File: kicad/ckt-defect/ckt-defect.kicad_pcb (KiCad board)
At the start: 2 copper layers, 99.1 x 61 mm, 67 parts, among them J1 Screw_Terminal_01x02, J10 Micro_SD_Card_Det_Hirose_DM3AT, J11 690-005-299-043, J12 SM04B-SRSS, J2 SM04B-SRSS, J3 SM04B-SRSS, J4 SM04B-SRSS, J5 SM04B-SRSS, J6 SM04B-SRSS, J7 SM04B-SRSS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

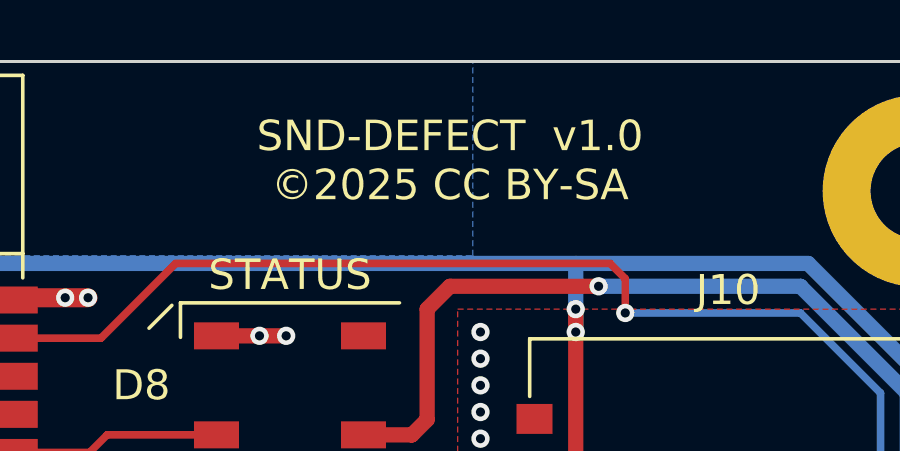
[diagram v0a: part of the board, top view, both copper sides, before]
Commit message: Renamed to ckt-defect
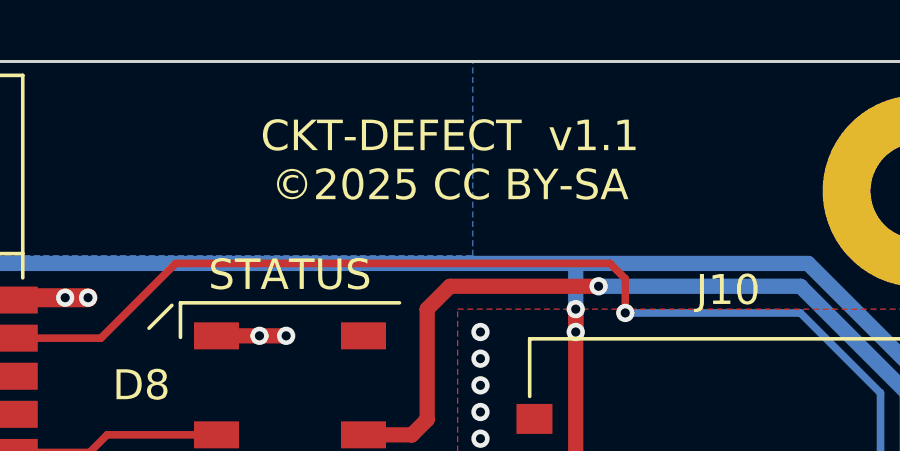
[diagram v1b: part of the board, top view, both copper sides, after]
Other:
- board text added: "CKT-DEFECT v1.1 ©2025 CC BY-SA"
- board text removed: "SND-DEFECT v1.0 ©2025 CC BY-SA"

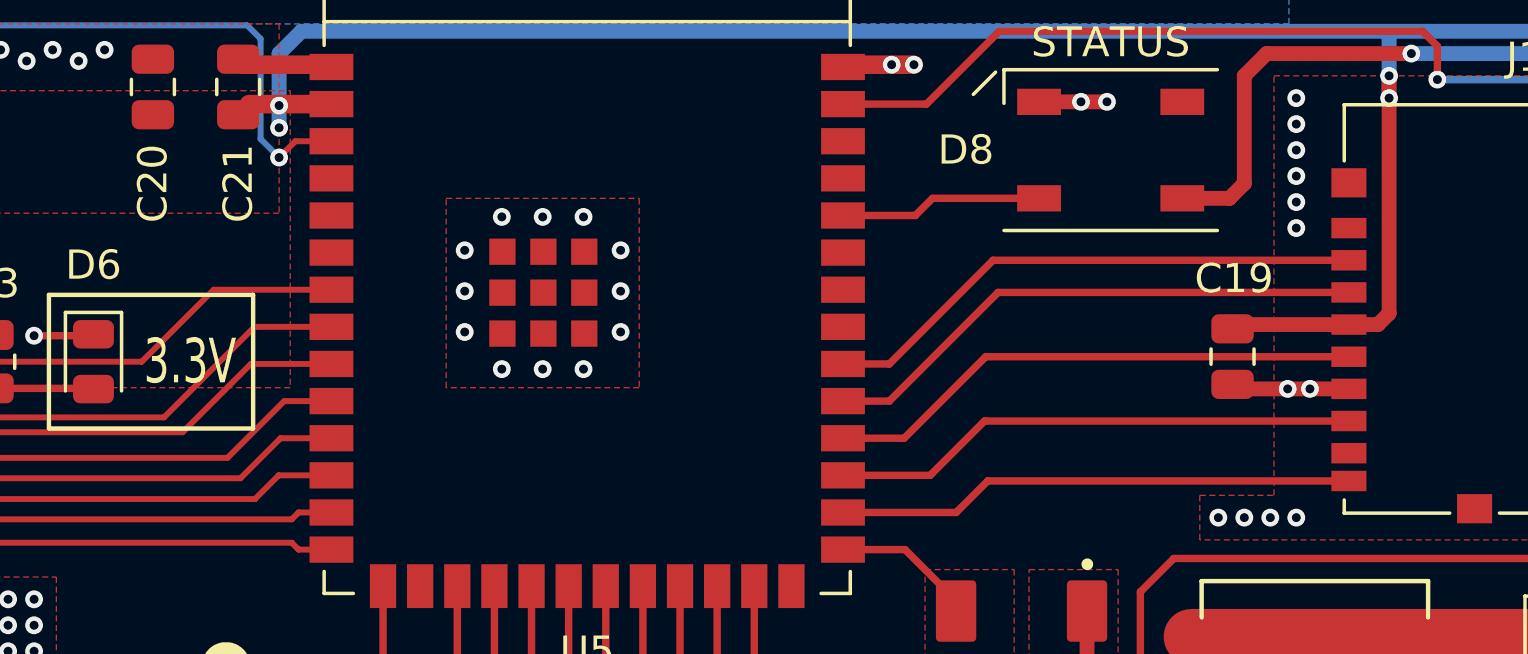
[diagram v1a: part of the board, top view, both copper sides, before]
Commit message: Kicad 9 conversion; added test points
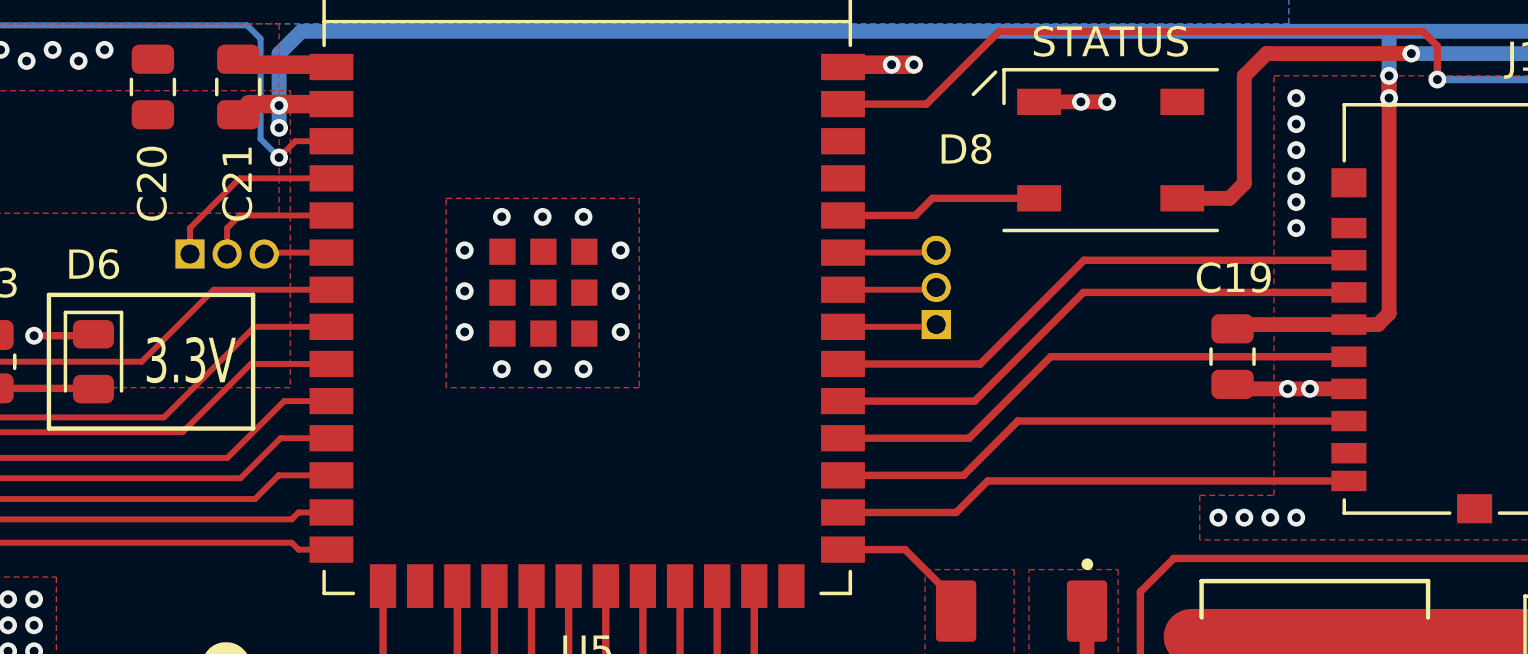
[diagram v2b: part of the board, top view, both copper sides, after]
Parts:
- added J13: Conn_01x03, Connector_PinHeader_1.27mm:PinHeader_1x03_P1.27mm_Vertical, F.Cu at (93.1, 65.2)
- added J14: Conn_01x03, Connector_PinHeader_1.27mm:PinHeader_1x03_P1.27mm_Vertical, F.Cu at (118.6, 67.6)
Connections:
- U5 pad 33: unconnected-(U5-Pad33) -> Net-(J14-Pin_1)
- U5 pad 34: unconnected-(U5-Pad34) -> Net-(J14-Pin_2)
- U5 pad 35: unconnected-(U5-Pad35) -> Net-(J14-Pin_3)
- U5 pad 4: unconnected-(U5-Pad4) -> Net-(J13-Pin_1)
- U5 pad 5: unconnected-(U5-Pad5) -> Net-(J13-Pin_2)
- U5 pad 6: unconnected-(U5-Pad6) -> Net-(J13-Pin_3)
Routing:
- net Net-(J13-Pin_1): track 0.00 -> 6.43 mm
- net Net-(J13-Pin_2): track 0.00 -> 4.64 mm
- net Net-(J14-Pin_3): track 0.00 -> 3.22 mm
- net Net-(J14-Pin_2): track 0.00 -> 3.22 mm
- net Net-(J14-Pin_1): track 0.00 -> 3.22 mm
- net Net-(J13-Pin_3): track 0.00 -> 2.32 mm

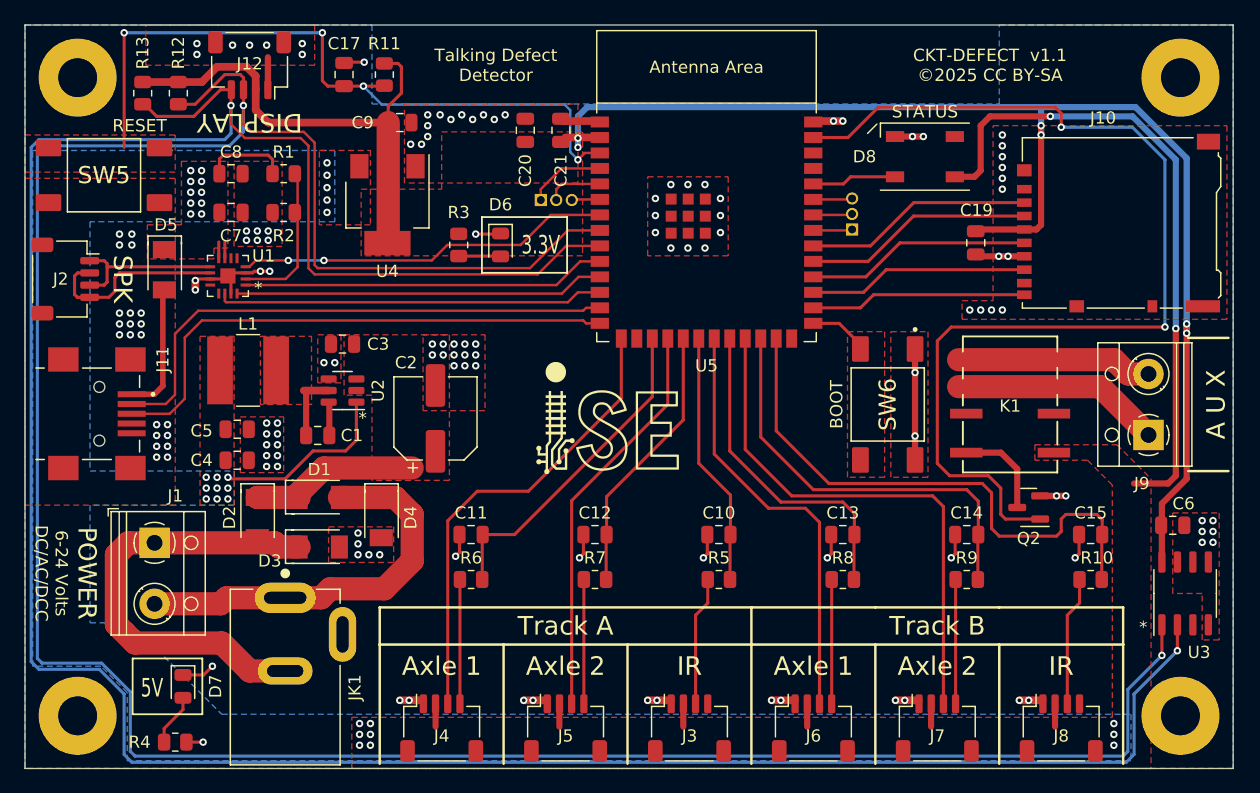
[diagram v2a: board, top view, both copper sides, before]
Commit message: Changed axle counters to use 3.3V supply
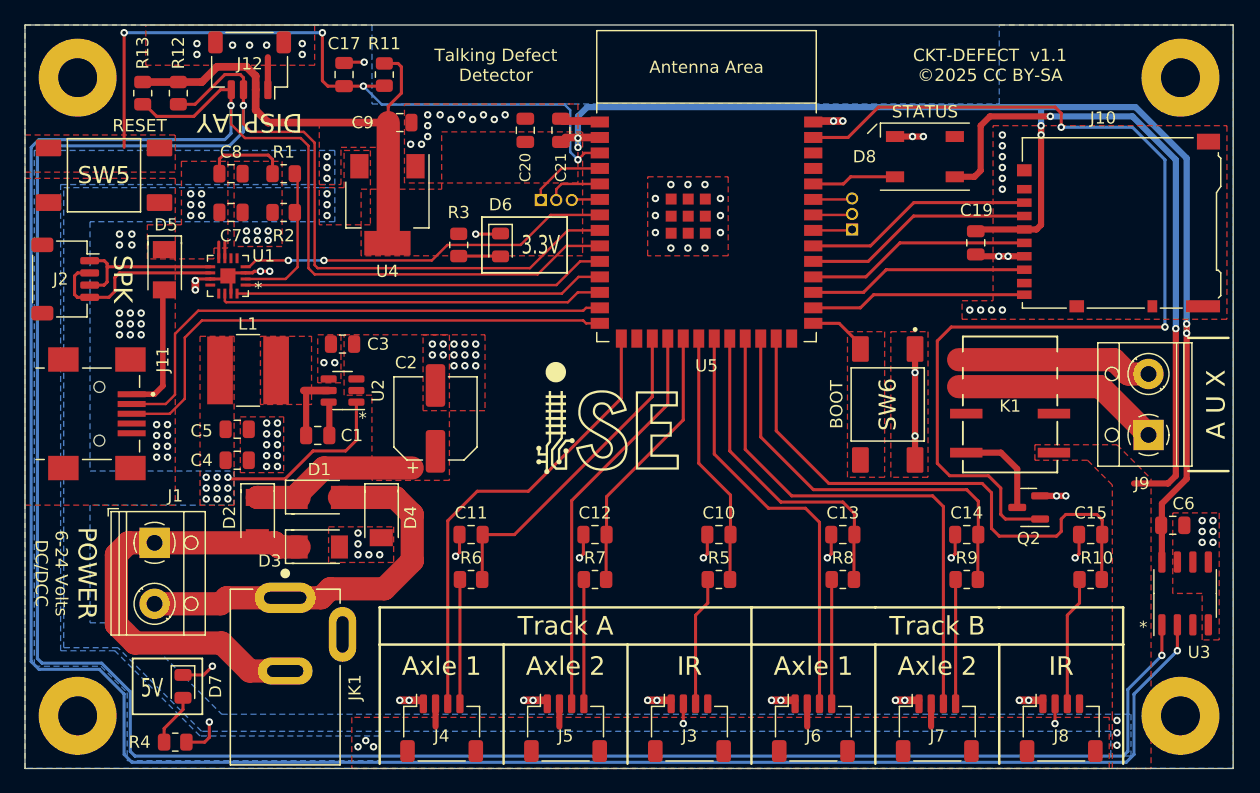
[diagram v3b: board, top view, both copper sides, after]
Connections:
- J3 pad MP: +5V -> +3.3V
- J4 pad 2: +5V -> +3.3V
- J4 pad MP: +5V -> +3.3V
- J5 pad 2: +5V -> +3.3V
- J5 pad MP: +5V -> +3.3V
- J6 pad 2: +5V -> +3.3V
- J6 pad MP: +5V -> +3.3V
- J7 pad 2: +5V -> +3.3V
- J7 pad MP: +5V -> +3.3V
- J8 pad MP: +5V -> +3.3V
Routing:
- net +3.3V: track 148.7 -> 156.2 mm, vias 6 -> 12
- net +5V: track 90.6 -> 84.6 mm, vias 36 -> 26
- added copper zone on B.Cu, net +3.3V
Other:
- board text added: "6-24 Volts DC/DCC"
- board text removed: "6-24 Volts DC/AC/DCC"

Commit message: Updated date
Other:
- board text added: "CKT-DEFECT v1.1 ©2026 CC BY-SA"
- board text removed: "CKT-DEFECT v1.1 ©2025 CC BY-SA"
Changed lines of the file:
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@@
 		)
 	)
-	(gr_text "CKT-DEFECT  v1.1\n©2025 CC BY-SA"
+	(gr_text "CKT-DEFECT  v1.1\n©2026 CC BY-SA"
 		(at 129.921 54.102 0)
 		(layer "F.SilkS")
